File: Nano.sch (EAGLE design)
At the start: 24 parts

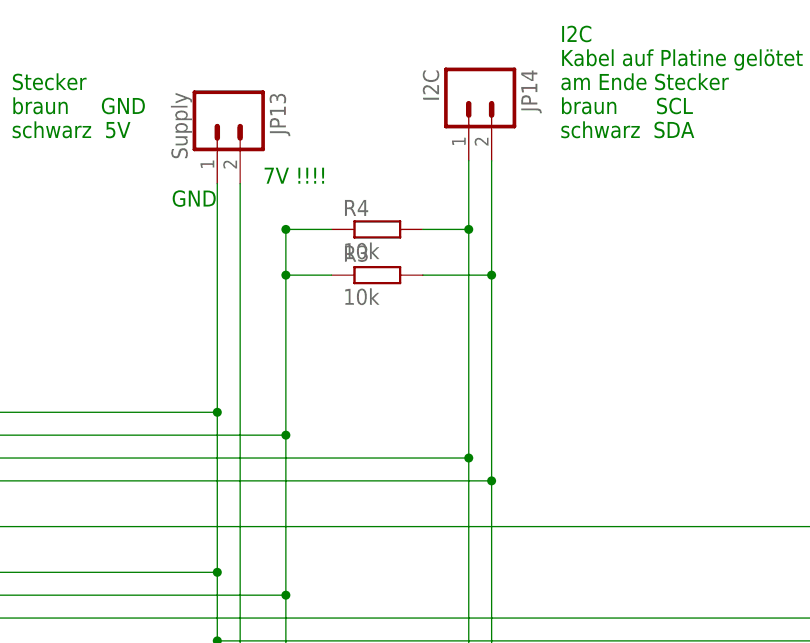
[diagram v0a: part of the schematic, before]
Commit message: 
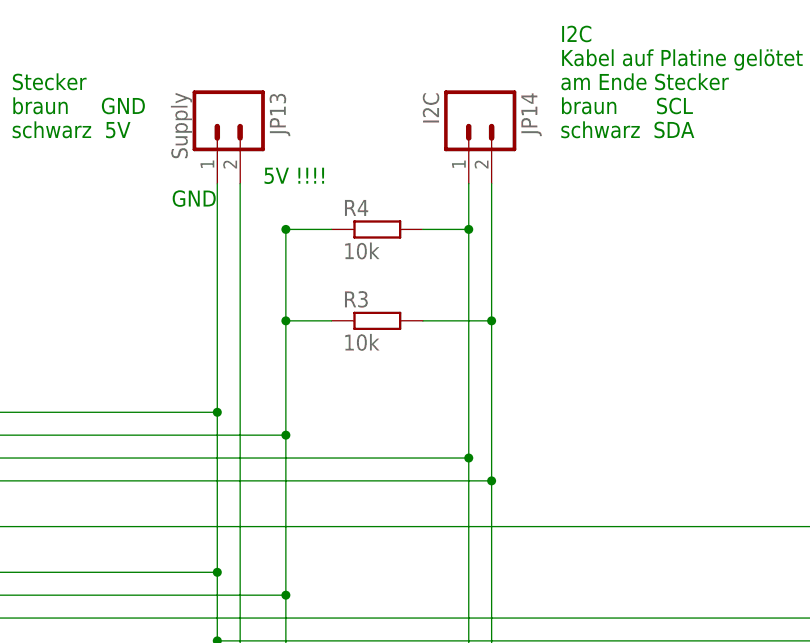
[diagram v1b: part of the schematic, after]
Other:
- note added: "5V !!!!"
- note removed: "7V !!!!"
- moved on the sheet: JP14, R3
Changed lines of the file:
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@@
 schwarz  5V</text>
 <text x="25.4" y="132.08" size="1.778" layer="91">GND</text>
-<text x="35.56" y="134.62" size="1.778" layer="91">7V !!!!</text>
+<text x="35.56" y="134.62" size="1.778" layer="91">5V !!!!</text>
 <text x="68.58" y="139.7" size="1.778" layer="91">I2C
 Kabel auf Platine gelötet
@@
 <instance part="LED2_BATT_LOW" gate="G$1" x="215.9" y="91.44" rot="R180"/>
 <instance part="R2" gate="G$1" x="215.9" y="73.66" rot="R90"/>
-<instance part="R3" gate="G$1" x="48.26" y="124.46"/>
+<instance part="R3" gate="G$1" x="48.26" y="119.38"/>
 <instance part="R4" gate="G$1" x="48.26" y="129.54"/>
 <instance part="JP8" gate="G$1" x="-101.6" y="104.14"/>
@@
 <instance part="JP7" gate="G$1" x="-83.82" y="40.64"/>
 <instance part="JP13" gate="G$1" x="30.48" y="142.24" rot="R270"/>
-<instance part="JP14" gate="G$1" x="58.42" y="144.78" rot="R270"/>
+<instance part="JP14" gate="G$1" x="58.42" y="142.24" rot="R270"/>
 <instance part="JP9" gate="G$1" x="129.54" y="66.04" rot="R180"/>
 </instances>
@@
 <wire x1="43.18" y1="129.54" x2="38.1" y2="129.54" width="0.1524" layer="91"/>
 <pinref part="R3" gate="G$1" pin="1"/>
-<wire x1="38.1" y1="124.46" x2="38.1" y2="106.68" width="0.1524" layer="91"/>
-<wire x1="43.18" y1="124.46" x2="38.1" y2="124.46" width="0.1524" layer="91"/>
-<wire x1="38.1" y1="124.46" x2="38.1" y2="129.54" width="0.1524" layer="91"/>
+<wire x1="38.1" y1="119.38" x2="38.1" y2="106.68" width="0.1524" layer="91"/>
+<wire x1="43.18" y1="119.38" x2="38.1" y2="119.38" width="0.1524" layer="91"/>
+<wire x1="38.1" y1="119.38" x2="38.1" y2="129.54" width="0.1524" layer="91"/>
 <junction x="38.1" y="129.54"/>
 <wire x1="-76.2" y1="106.68" x2="38.1" y2="106.68" width="0.1524" layer="91"/>
@@
 <pinref part="JP7" gate="G$1" pin="3"/>
 <wire x1="-76.2" y1="43.18" x2="-10.16" y2="43.18" width="0.1524" layer="91"/>
-<junction x="38.1" y="124.46"/>
+<junction x="38.1" y="119.38"/>
 <wire x1="33.02" y1="66.04" x2="38.1" y2="66.04" width="0.1524" layer="91"/>
 <junction x="38.1" y="66.04"/>
@@
 <wire x1="66.04" y1="58.42" x2="60.96" y2="58.42" width="0.1524" layer="91"/>
 <wire x1="60.96" y1="58.42" x2="60.96" y2="101.6" width="0.1524" layer="91"/>
-<wire x1="60.96" y1="101.6" x2="60.96" y2="124.46" width="0.1524" layer="91"/>
+<wire x1="60.96" y1="101.6" x2="60.96" y2="119.38" width="0.1524" layer="91"/>
 <junction x="60.96" y="101.6"/>
 <pinref part="JP11" gate="G$1" pin="1"/>
-<wire x1="60.96" y1="124.46" x2="60.96" y2="137.16" width="0.1524" layer="91"/>
+<wire x1="60.96" y1="119.38" x2="60.96" y2="134.62" width="0.1524" layer="91"/>
 <wire x1="-76.2" y1="101.6" x2="60.96" y2="101.6" width="0.1524" layer="91"/>
 <pinref part="JP14" gate="G$1" pin="2"/>
 <pinref part="R3" gate="G$1" pin="2"/>
-<wire x1="60.96" y1="124.46" x2="53.34" y2="124.46" width="0.1524" layer="91"/>
-<junction x="60.96" y="124.46"/>
+<wire x1="60.96" y1="119.38" x2="53.34" y2="119.38" width="0.1524" layer="91"/>
+<junction x="60.96" y="119.38"/>
 </segment>
 </net>
@@
 <wire x1="58.42" y1="104.14" x2="58.42" y2="129.54" width="0.1524" layer="91"/>
 <pinref part="R4" gate="G$1" pin="2"/>
-<wire x1="58.42" y1="129.54" x2="58.42" y2="137.16" width="0.1524" layer="91"/>
+<wire x1="58.42" y1="129.54" x2="58.42" y2="134.62" width="0.1524" layer="91"/>
 <wire x1="58.42" y1="129.54" x2="53.34" y2="129.54" width="0.1524" layer="91"/>
 <junction x="58.42" y="129.54"/>

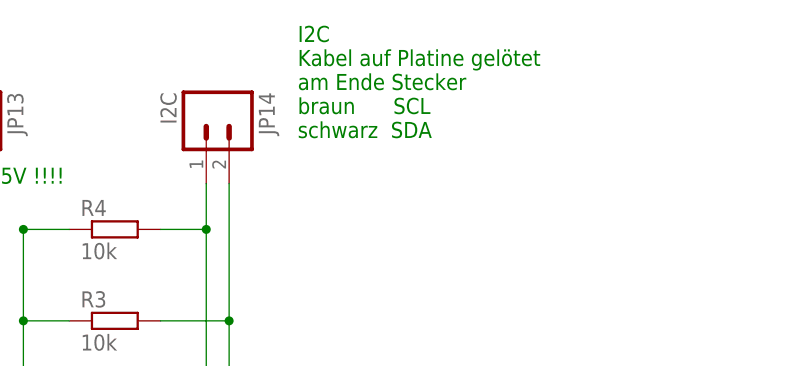
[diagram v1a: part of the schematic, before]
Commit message: 
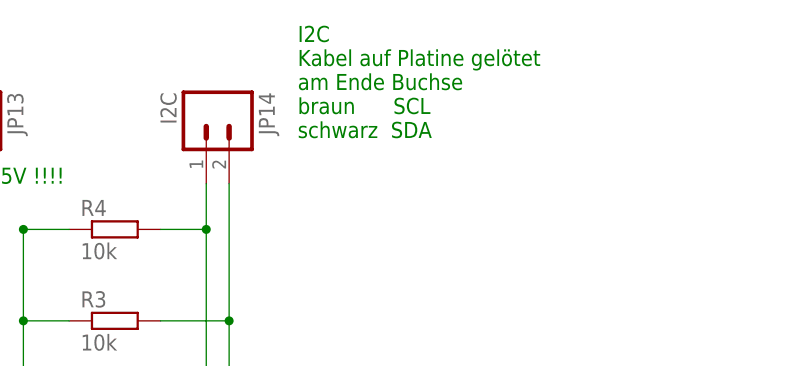
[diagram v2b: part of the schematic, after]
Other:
- note added: "I2C Kabel auf Platine gelötet am Ende Buchse braun SCL schwarz SDA"
- note removed: "I2C Kabel auf Platine gelötet am Ende Stecker braun SCL schwarz SDA"
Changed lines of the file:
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@@
 <text x="68.58" y="139.7" size="1.778" layer="91">I2C
 Kabel auf Platine gelötet
-am Ende Stecker
+am Ende Buchse
 braun      SCL
 schwarz  SDA</text>

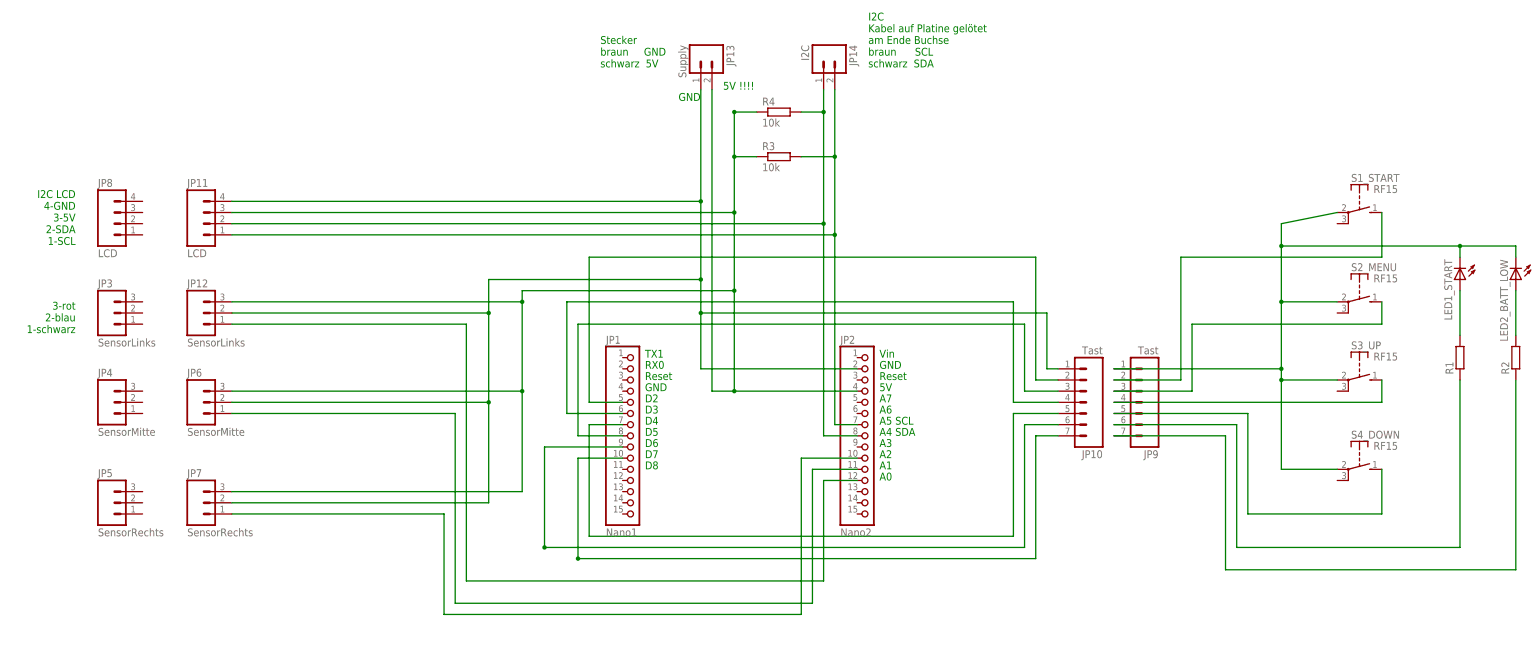
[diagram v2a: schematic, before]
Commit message: 
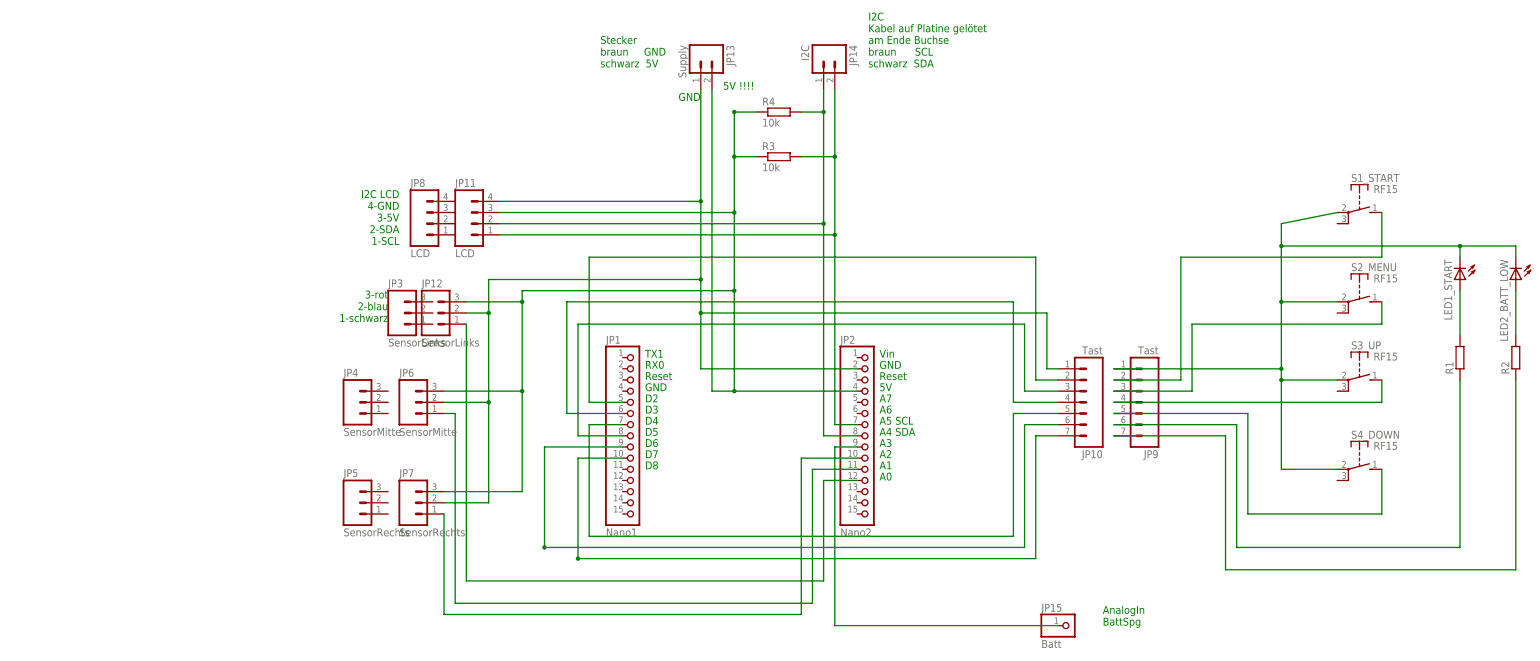
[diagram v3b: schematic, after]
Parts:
- added JP15: Batt, pinhead:PINHD-1X1
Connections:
- new net N$6: JP15.1, JP2.9
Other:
- note added: "AnalogIn BattSpg"
- moved on the sheet: JP11, JP12, JP3, JP4, JP5, JP6, JP7, JP8
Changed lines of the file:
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@@
 <?xml version="1.0" encoding="utf-8"?>
 <!DOCTYPE eagle SYSTEM "eagle.dtd">
-<eagle version="7.7.0">
+<eagle version="8.5.1">
 <drawing>
 <settings>
 <setting alwaysvectorfont="no"/>
+<setting keepoldvectorfont="yes"/>
 <setting verticaltext="up"/>
 </settings>
@@
 <layer number="223" name="223bmp" color="24" fill="1" visible="no" active="no"/>
 <layer number="224" name="224bmp" color="25" fill="1" visible="no" active="no"/>
+<layer number="225" name="225bmp" color="7" fill="1" visible="yes" active="yes"/>
+<layer number="226" name="226bmp" color="7" fill="1" visible="yes" active="yes"/>
+<layer number="227" name="227bmp" color="7" fill="1" visible="yes" active="yes"/>
+<layer number="228" name="228bmp" color="7" fill="1" visible="yes" active="yes"/>
+<layer number="229" name="229bmp" color="7" fill="1" visible="yes" active="yes"/>
+<layer number="230" name="230bmp" color="7" fill="1" visible="yes" active="yes"/>
 <layer number="231" name="Eagle3D_PG1" color="7" fill="1" visible="no" active="no"/>
 <layer number="232" name="Eagle3D_PG2" color="7" fill="1" visible="no" active="no"/>
@@
 <part name="JP14" library="SparkFun-Connectors" deviceset="M02" device="LOCK" value="I2C"/>
 <part name="JP9" library="SparkFun-Connectors" deviceset="M07" device="" value="Tast"/>
+<part name="JP15" library="pinhead" deviceset="PINHD-1X1" device="" value="Batt"/>
+<part name="FRAME1" library="SparkFun-Aesthetics" deviceset="FRAME-A4L" device=""/>
 </parts>
 <sheets>
@@
 braun      SCL
 schwarz  SDA</text>
-<text x="-111.76" y="111.76" size="1.778" layer="91" rot="R180">I2C LCD
+<text x="-38.1" y="111.76" size="1.778" layer="91" rot="R180">I2C LCD
 4-GND
 3-5V
 2-SDA
 1-SCL</text>
-<text x="-111.76" y="86.36" size="1.778" layer="91" rot="R180">3-rot
+<text x="-40.64" y="88.9" size="1.778" layer="91" rot="R180">3-rot
 2-blau
 1-schwarz</text>
+<text x="121.92" y="12.7" size="1.778" layer="91">AnalogIn
+BattSpg</text>
 </plain>
 <instances>
 <instance part="JP1" gate="A" x="15.24" y="55.88"/>
 <instance part="JP2" gate="A" x="68.58" y="55.88"/>
-<instance part="JP3" gate="G$1" x="-104.14" y="83.82"/>
-<instance part="JP4" gate="G$1" x="-104.14" y="63.5"/>
-<instance part="JP5" gate="G$1" x="-104.14" y="40.64"/>
+<instance part="JP3" gate="G$1" x="-38.1" y="83.82"/>
+<instance part="JP4" gate="G$1" x="-48.26" y="63.5"/>
+<instance part="JP5" gate="G$1" x="-48.26" y="40.64"/>
 <instance part="S1_START" gate="1" x="180.34" y="106.68" rot="R270"/>
 <instance part="S2_MENU" gate="1" x="180.34" y="86.36" rot="R270"/>
@@
 <instance part="R3" gate="G$1" x="48.26" y="119.38"/>
 <instance part="R4" gate="G$1" x="48.26" y="129.54"/>
-<instance part="JP8" gate="G$1" x="-101.6" y="104.14"/>
+<instance part="JP8" gate="G$1" x="-30.48" y="104.14"/>
 <instance part="JP10" gate="G$1" x="116.84" y="66.04" rot="R180"/>
-<instance part="JP11" gate="G$1" x="-81.28" y="104.14"/>
-<instance part="JP12" gate="G$1" x="-83.82" y="83.82"/>
-<instance part="JP6" gate="G$1" x="-83.82" y="63.5"/>
-<instance part="JP7" gate="G$1" x="-83.82" y="40.64"/>
+<instance part="JP11" gate="G$1" x="-20.32" y="104.14"/>
+<instance part="JP12" gate="G$1" x="-30.48" y="83.82"/>
+<instance part="JP6" gate="G$1" x="-35.56" y="63.5"/>
+<instance part="JP7" gate="G$1" x="-35.56" y="40.64"/>
 <instance part="JP13" gate="G$1" x="30.48" y="142.24" rot="R270"/>
 <instance part="JP14" gate="G$1" x="58.42" y="142.24" rot="R270"/>
 <instance part="JP9" gate="G$1" x="129.54" y="66.04" rot="R180"/>
+<instance part="JP15" gate="G$1" x="114.3" y="12.7"/>
+<instance part="FRAME1" gate="G$1" x="-53.34" y="-20.32"/>
 </instances>
 <busses>
@@
 <net name="N$11" class="0">
 <segment>
-<wire x1="-76.2" y1="81.28" x2="-22.86" y2="81.28" width="0.1524" layer="91"/>
 <wire x1="-22.86" y1="81.28" x2="-22.86" y2="22.86" width="0.1524" layer="91"/>
 <wire x1="-22.86" y1="22.86" x2="58.42" y2="22.86" width="0.1524" layer="91"/>
@@
 <net name="N$12" class="0">
 <segment>
-<wire x1="-76.2" y1="60.96" x2="-25.4" y2="60.96" width="0.1524" layer="91"/>
+<wire x1="-27.94" y1="60.96" x2="-25.4" y2="60.96" width="0.1524" layer="91"/>
 <wire x1="-25.4" y1="60.96" x2="-25.4" y2="17.78" width="0.1524" layer="91"/>
 <wire x1="-25.4" y1="17.78" x2="55.88" y2="17.78" width="0.1524" layer="91"/>
@@
 <net name="N$13" class="0">
 <segment>
-<wire x1="-76.2" y1="38.1" x2="-27.94" y2="38.1" width="0.1524" layer="91"/>
 <wire x1="-27.94" y1="38.1" x2="-27.94" y2="15.24" width="0.1524" layer="91"/>
 <wire x1="-27.94" y1="15.24" x2="53.34" y2="15.24" width="0.1524" layer="91"/>
@@
 <wire x1="33.02" y1="66.04" x2="33.02" y2="134.62" width="0.1524" layer="91"/>
 <pinref part="JP13" gate="G$1" pin="2"/>
-<wire x1="-76.2" y1="86.36" x2="-10.16" y2="86.36" width="0.1524" layer="91"/>
+<wire x1="-22.86" y1="86.36" x2="-10.16" y2="86.36" width="0.1524" layer="91"/>
 <pinref part="JP12" gate="G$1" pin="3"/>
 <pinref part="JP2" gate="A" pin="4"/>
-<wire x1="-76.2" y1="66.04" x2="-10.16" y2="66.04" width="0.1524" layer="91"/>
+<wire x1="-27.94" y1="66.04" x2="-10.16" y2="66.04" width="0.1524" layer="91"/>
 <wire x1="66.04" y1="66.04" x2="38.1" y2="66.04" width="0.1524" layer="91"/>
 <pinref part="R4" gate="G$1" pin="1"/>
@@
 <wire x1="38.1" y1="119.38" x2="38.1" y2="129.54" width="0.1524" layer="91"/>
 <junction x="38.1" y="129.54"/>
-<wire x1="-76.2" y1="106.68" x2="38.1" y2="106.68" width="0.1524" layer="91"/>
+<wire x1="-15.24" y1="106.68" x2="38.1" y2="106.68" width="0.1524" layer="91"/>
 <pinref part="JP11" gate="G$1" pin="3"/>
 <junction x="38.1" y="106.68"/>
@@
 <pinref part="JP6" gate="G$1" pin="3"/>
 <pinref part="JP7" gate="G$1" pin="3"/>
-<wire x1="-76.2" y1="43.18" x2="-10.16" y2="43.18" width="0.1524" layer="91"/>
+<wire x1="-27.94" y1="43.18" x2="-10.16" y2="43.18" width="0.1524" layer="91"/>
 <junction x="38.1" y="119.38"/>
 <wire x1="33.02" y1="66.04" x2="38.1" y2="66.04" width="0.1524" layer="91"/>
@@
 <net name="N$22" class="0">
 <segment>
-<wire x1="-76.2" y1="109.22" x2="30.48" y2="109.22" width="0.1524" layer="91"/>
+<wire x1="-15.24" y1="109.22" x2="30.48" y2="109.22" width="0.1524" layer="91"/>
 <pinref part="JP11" gate="G$1" pin="4"/>
 <pinref part="JP2" gate="A" pin="2"/>
@@
 <junction x="30.48" y="83.82"/>
 <junction x="30.48" y="109.22"/>
-<wire x1="-76.2" y1="40.64" x2="-17.78" y2="40.64" width="0.1524" layer="91"/>
+<wire x1="-27.94" y1="40.64" x2="-17.78" y2="40.64" width="0.1524" layer="91"/>
 <wire x1="-17.78" y1="40.64" x2="-17.78" y2="63.5" width="0.1524" layer="91"/>
 <wire x1="-17.78" y1="63.5" x2="-17.78" y2="83.82" width="0.1524" layer="91"/>
@@
 <wire x1="30.48" y1="91.44" x2="-17.78" y2="91.44" width="0.1524" layer="91"/>
 <pinref part="JP12" gate="G$1" pin="2"/>
-<wire x1="-76.2" y1="63.5" x2="-17.78" y2="63.5" width="0.1524" layer="91"/>
-<wire x1="-76.2" y1="83.82" x2="-17.78" y2="83.82" width="0.1524" layer="91"/>
+<wire x1="-27.94" y1="63.5" x2="-17.78" y2="63.5" width="0.1524" layer="91"/>
+<wire x1="-22.86" y1="83.82" x2="-17.78" y2="83.82" width="0.1524" layer="91"/>
 <junction x="-17.78" y="63.5"/>
 <junction x="-17.78" y="83.82"/>
@@
 <pinref part="JP11" gate="G$1" pin="1"/>
 <wire x1="60.96" y1="119.38" x2="60.96" y2="134.62" width="0.1524" layer="91"/>
-<wire x1="-76.2" y1="101.6" x2="60.96" y2="101.6" width="0.1524" layer="91"/>
+<wire x1="-15.24" y1="101.6" x2="60.96" y2="101.6" width="0.1524" layer="91"/>
 <pinref part="JP14" gate="G$1" pin="2"/>
 <pinref part="R3" gate="G$1" pin="2"/>
@@
 <junction x="58.42" y="104.14"/>
 <pinref part="JP11" gate="G$1" pin="2"/>
-<wire x1="-76.2" y1="104.14" x2="58.42" y2="104.14" width="0.1524" layer="91"/>
+<wire x1="-15.24" y1="104.14" x2="58.42" y2="104.14" width="0.1524" layer="91"/>
 <pinref part="JP14" gate="G$1" pin="1"/>
 </segment>
@@
 </segment>
 </net>
+<net name="N$6" class="0">
+<segment>
+<pinref part="JP15" gate="G$1" pin="1"/>
+<wire x1="111.76" y1="12.7" x2="60.96" y2="12.7" width="0.1524" layer="91"/>
+<pinref part="JP2" gate="A" pin="9"/>
+<wire x1="66.04" y1="53.34" x2="60.96" y2="53.34" width="0.1524" layer="91"/>
+<wire x1="60.96" y1="53.34" x2="60.96" y2="12.7" width="0.1524" layer="91"/>
+</segment>
+</net>
